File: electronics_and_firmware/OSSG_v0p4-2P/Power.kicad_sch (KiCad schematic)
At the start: 37 parts, among them J3 USB_B_Micro, Q3 PMZ290UNE2YL, Q4 EMF20B02V, SW2 Power, U4 XC61CC3002MR, U5 AP5054HTC, U6 MAX17048, U7 NCP167BMX330TBG, U8 SY7088

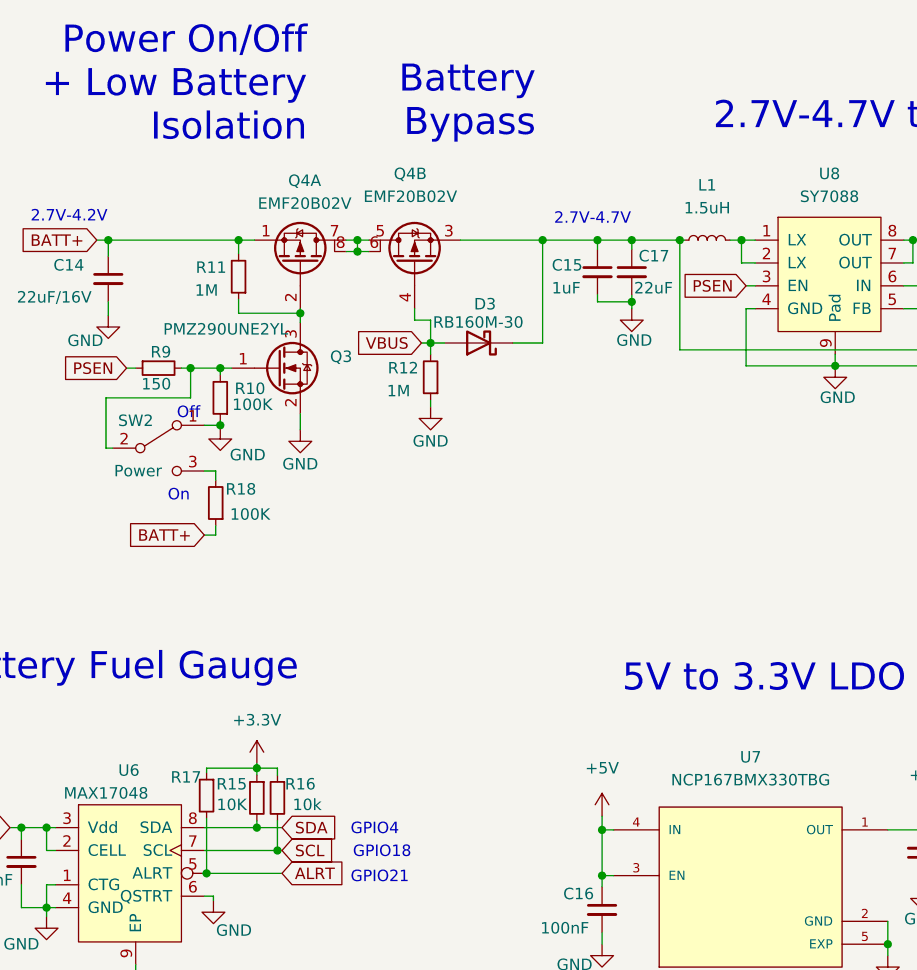
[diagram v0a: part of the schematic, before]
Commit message: V0.4 PCB nearly finished.  3D models mostly added in. Needs reviewing
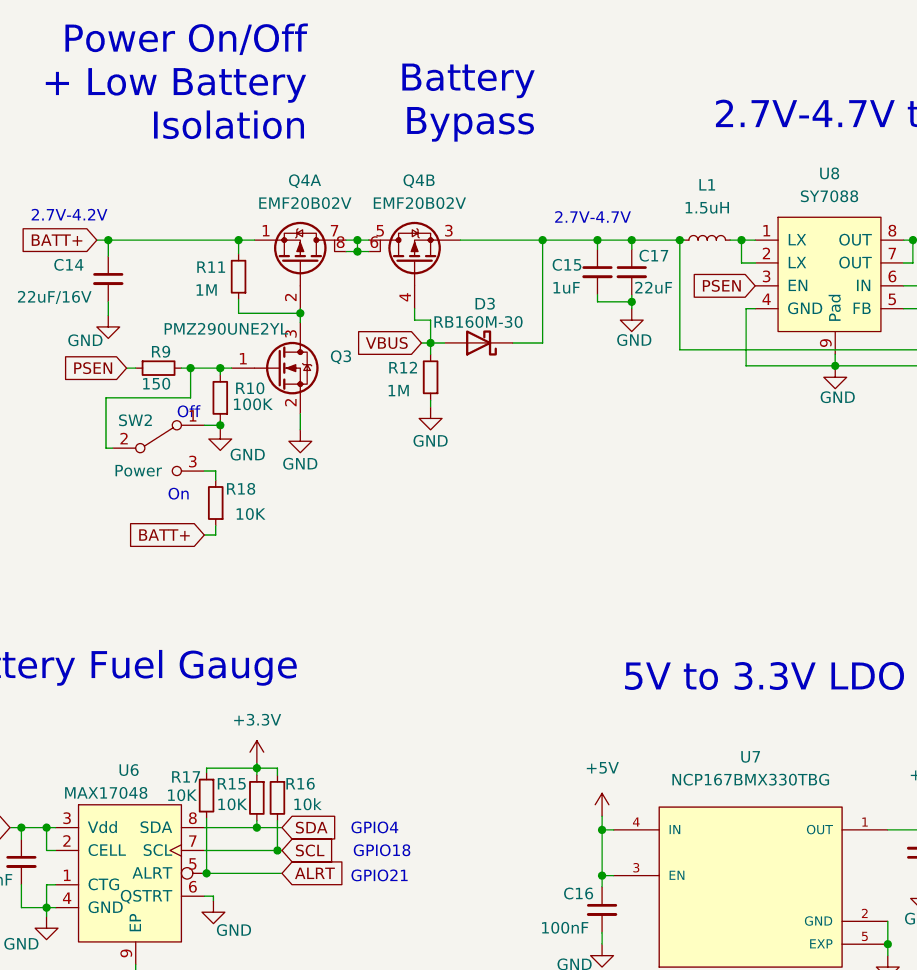
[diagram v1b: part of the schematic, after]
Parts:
- R17: value (none) -> 10K; footprint (none) -> Resistor_SMD:R_0402_1005Metric
- R18: value 100K -> 10K
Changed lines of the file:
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@@
-    (stroke (width 0) (type default) (color 0 0 0 0))
-  )
-  (wire (pts (xy 219.456 68.58) (xy 220.472 68.58))
     (stroke (width 0) (type default) (color 0 0 0 0))
   )
@@
     )
   )
-  (global_label "PSEN" (shape input) (at 219.456 68.58 180) (fields_autoplaced)
+  (global_label "PSEN" (shape input) (at 220.472 68.58 180) (fields_autoplaced)
     (effects (font (size 1.27 1.27)) (justify right))
-    (property "Intersheet References" "${INTERSHEET_REFS}" (id 0) (at 212.0839 68.5006 0)
+    (property "Intersheet References" "${INTERSHEET_REFS}" (id 0) (at 213.0999 68.5006 0)
       (effects (font (size 1.27 1.27)) (justify right) hide)
     )
@@
   )
   (symbol (lib_id "OSSG_components_lib:EMF20B02V") (at 182.626 66.04 90) (unit 2)
-    (in_bom yes) (on_board yes) (fields_autoplaced)
-    (property "Reference" "Q4" (id 0) (at 182.1434 56.134 90))
-    (property "Value" "EMF20B02V" (id 1) (at 182.1434 58.674 90))
+    (in_bom yes) (on_board yes)
+    (property "Reference" "Q4" (id 0) (at 183.134 56.896 90))
+    (property "Value" "EMF20B02V" (id 1) (at 183.134 59.436 90))
     (property "Footprint" "OSSG_footprints:EMF20B02V" (id 2) (at 182.626 64.77 0)
       (effects (font (size 1.27 1.27)) hide)
@@
     (in_bom yes) (on_board yes)
     (property "Reference" "R18" (id 0) (at 163.322 91.186 0))
-    (property "Value" "100K" (id 1) (at 164.338 93.98 0))
+    (property "Value" "10K" (id 1) (at 164.338 93.98 0))
     (property "Footprint" "Resistor_SMD:R_0402_1005Metric" (id 2) (at 160.528 92.71 0)
       (effects (font (size 1.27 1.27)) hide)
@@
     (in_bom yes) (on_board yes)
     (property "Reference" "R17" (id 0) (at 157.226 123.19 0))
-    (property "Value" "" (id 1) (at 156.718 125.222 0))
-    (property "Footprint" "" (id 2) (at 159.512 125.222 0)
-      (effects (font (size 1.27 1.27)) hide)
-    )
+    (property "Value" "10K" (id 1) (at 156.718 125.222 0))
+    (property "Footprint" "Resistor_SMD:R_0402_1005Metric" (id 2) (at 159.512 125.222 0)
+      (effects (font (size 1.27 1.27)) hide)
+    )

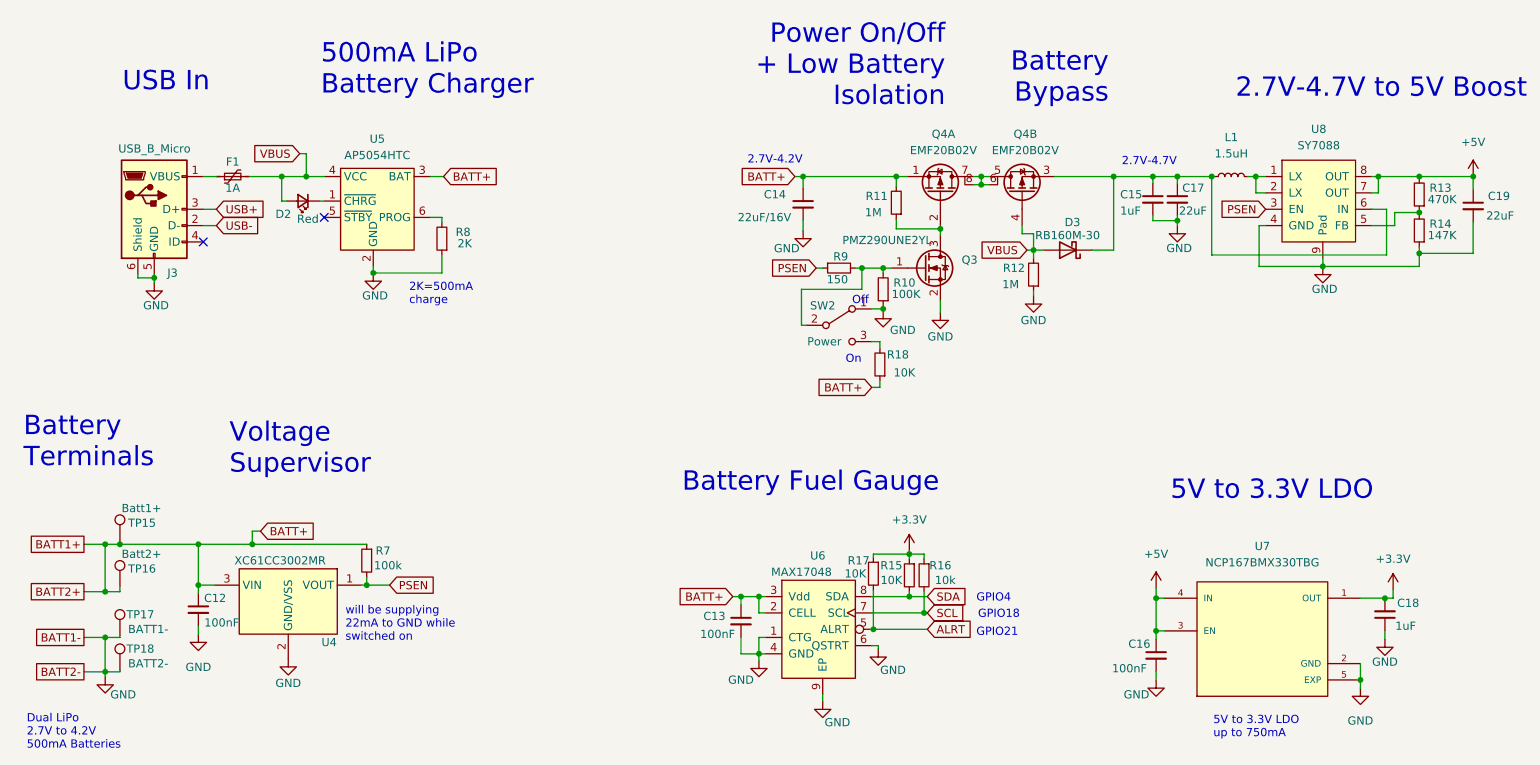
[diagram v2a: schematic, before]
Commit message: change Q4 footprint
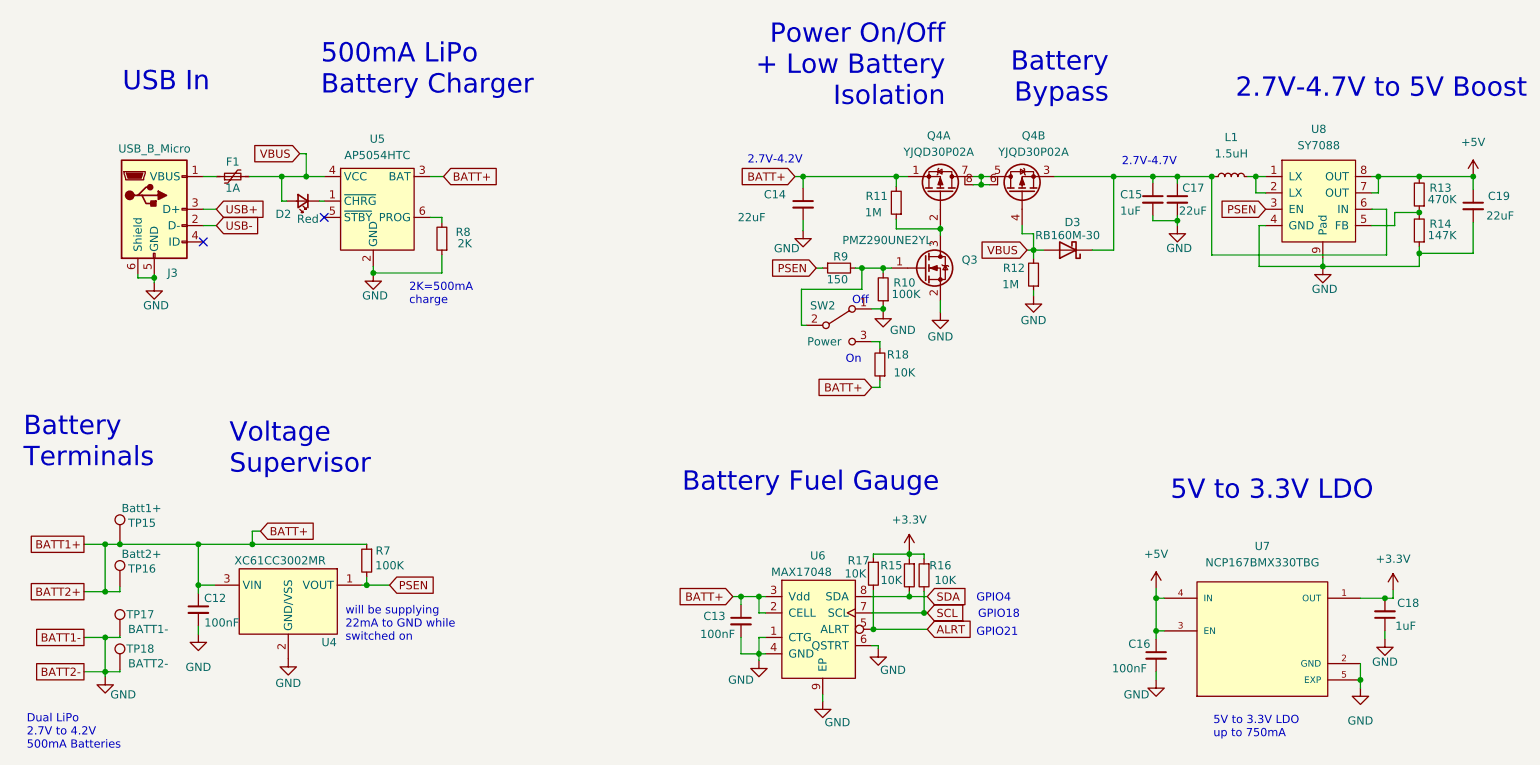
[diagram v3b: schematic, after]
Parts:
- removed Q4: EMF20B02V, OSSG_footprints:EMF20B02V, symbol OSSG_components_lib:EMF20B02V
- added Q4: YJQD30P02A, OSSG_footprints:YJQD30P02A_DFN3.3x3.3, symbol OSSG_components_lib:YJQD30P02A
- C14: value 22uF/16V -> 22uF
- R16: value 10k -> 10K
- R7: value 100k -> 100K
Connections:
- net BATT+: now also Q4.1 (S2)
- net VBUS: now also Q4.4 (G2)
- net at C15.1, C17.1, D3.1 (K)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: now also Q4.3 (S2)
- net at Q3.3 (D), R11.1: now also Q4.2 (G2)
- new net: Q4.5 (D2), Q4.6 (D2), Q4.7 (D2), Q4.8 (D2)
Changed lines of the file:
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@@
   (title_block
     (title "Team OpenSource Smartglasses")
-    (date "2022-09-18")
-    (rev "V0.4b4")
+    (date "2022-09-19")
+    (rev "V0.4b5")
     (comment 1 "2P Battery Version")
     (comment 2 "MIT License")
@@
     (pin "1")
   )
-  (symbol (lib_id "OSSG_components_lib:EMF20B02V") (at 169.926 66.04 270) (mirror x) (unit 1)
-    (in_bom yes) (on_board yes) (fields_autoplaced)
-    (property "Reference" "Q4" (id 0) (at 170.4086 56.896 90))
-    (property "Value" "EMF20B02V" (id 1) (at 170.4086 59.436 90))
-    (property "Footprint" "OSSG_footprints:EMF20B02V" (id 2) (at 169.926 64.77 0)
-      (effects (font (size 1.27 1.27)) hide)
-    )
-    (property "Datasheet" "~" (id 3) (at 169.926 64.77 0)
-      (effects (font (size 1.27 1.27)) hide)
-    )
-    (pin "1")
-    (pin "2")
-    (pin "7")
-    (pin "8")
-    (pin "3")
-    (pin "4")
-    (pin "5")
-    (pin "6")
-  )
   (symbol (lib_id "Device:C_Small") (at 138.938 132.588 0) (unit 1)
     (in_bom yes) (on_board yes)
@@
     (in_bom yes) (on_board yes)
     (property "Reference" "R16" (id 0) (at 169.926 123.952 0))
-    (property "Value" "10k" (id 1) (at 170.688 126.238 0))
+    (property "Value" "10K" (id 1) (at 170.688 126.238 0))
     (property "Footprint" "Resistor_SMD:R_0402_1005Metric" (id 2) (at 167.386 125.476 0)
       (effects (font (size 1.27 1.27)) hide)
@@
     (pin "1")
   )
-  (symbol (lib_id "OSSG_components_lib:EMF20B02V") (at 182.626 66.04 90) (unit 2)
-    (in_bom yes) (on_board yes)
-    (property "Reference" "Q4" (id 0) (at 183.134 56.896 90))
-    (property "Value" "EMF20B02V" (id 1) (at 183.134 59.436 90))
-    (property "Footprint" "OSSG_footprints:EMF20B02V" (id 2) (at 182.626 64.77 0)
+  (symbol (lib_id "OSSG_components_lib:YJQD30P02A") (at 182.626 66.04 90) (unit 2)
+    (in_bom yes) (on_board yes)
+    (property "Reference" "Q4" (id 0) (at 184.404 57.15 90))
+    (property "Value" "YJQD30P02A" (id 1) (at 184.404 59.69 90))
+    (property "Footprint" "OSSG_footprints:YJQD30P02A_DFN3.3x3.3" (id 2) (at 182.626 64.77 0)
       (effects (font (size 1.27 1.27)) hide)
     )
@@
     (in_bom yes) (on_board yes)
     (property "Reference" "R7" (id 0) (at 83.312 121.666 0))
-    (property "Value" "100k" (id 1) (at 84.074 123.952 0))
+    (property "Value" "100K" (id 1) (at 84.328 123.952 0))
     (property "Footprint" "Resistor_SMD:R_0402_1005Metric" (id 2) (at 80.772 123.19 0)
       (effects (font (size 1.27 1.27)) hide)
@@
     (pin "2")
   )
-  (symbol (lib_id "power:GND") (at 169.926 84.582 0) (unit 1)
-    (in_bom yes) (on_board yes)
-    (property "Reference" "#PWR037" (id 0) (at 169.926 90.932 0)
-      (effects (font (size 1.27 1.27)) hide)
-    )
-    (property "Value" "GND" (id 1) (at 169.926 88.392 0))
-    (property "Footprint" "" (id 2) (at 169.926 84.582 0)
-      (effects (font (size 1.27 1.27)) hide)
-    )
-    (property "Datasheet" "" (id 3) (at 169.926 84.582 0)
-      (effects (font (size 1.27 1.27)) hide)
-    )
-    (pin "1")
-  )
-  (symbol (lib_id "Connector:USB_B_Micro") (at 47.752 68.58 0) (unit 1)
-    (in_bom yes) (on_board yes)
-    (property "Reference" "J3" (id 0) (at 49.784 78.486 0)
-      (effects (font (size 1.27 1.27)) (justify left))
-    )
-    (property "Value" "USB_B_Micro" (id 1) (at 42.164 59.182 0)
-      (effects (font (size 1.27 1.27)) (justify left))
-    )
-    (property "Footprint" "Connector_USB:USB_Micro-B_Amphenol_10118194_Horizontal" (id 2) (at 51.562 69.85 0)
-      (effects (font (size 1.27 1.27)) hide)
-    )
-    (property "Datasheet" "https://www.molex.com/pdm_docs/sd/1050170001_sd.pdf" (id 3) (at 51.562 69.85 0)
-      (effects (font (size 1.27 1.27)) hide)
-    )
-    (property "MPN" "WM1399CT-ND" (id 4) (at 47.752 68.58 90)
-      (effects (font (size 1.27 1.27)) hide)
-    )
-    (property "Price" "1.33" (id 5) (at 47.752 68.58 90)
-      (effects (font (size 1.27 1.27)) hide)
-    )
-    (property "DigiKeyLink" "https://www.digikey.ca/en/products/detail/molex/1050170001/2350832" (id 6) (at 47.752 68.58 90)
-      (effects (font (size 1.27 1.27)) hide)
-    )
-    (property "Price_LCSC" "0.244" (id 7) (at 47.752 68.58 90)
-      (effects (font (size 1.27 1.27)) hide)
-    )
-    (property "LinkLCSC" "https://lcsc.com/product-detail/USB-Connectors_MOLEX-1050170001_C136000.html" (id 8) (at 47.752 68.58 90)
-      (effects (font (size 1.27 1.27)) hide)
-    )
-    (property "MPN_LCSC" "C136000" (id 9) (at 47.752 68.58 90)
-      (effects (font (size 1.27 1.27)) hide)
-    )
-    (pin "1")
-    (pin "2")
+  (symbol (lib_id "OSSG_components_lib:YJQD30P02A") (at 169.926 66.04 270) (mirror x) (unit 1)
+    (in_bom yes) (on_board yes)
+    (property "Reference" "Q4" (id 0) (at 169.672 57.15 90))
+    (property "Value" "YJQD30P02A" (id 1) (at 169.672 59.69 90))
+    (property "Footprint" "OSSG_footprints:YJQD30P02A_DFN3.3x3.3" (id 2) (at 169.926 64.77 0)
+      (effects (font (size 1.27 1.27)) hide)
+    )
+    (property "Datasheet" "~" (id 3) (at 169.926 64.77 0)
+      (effects (font (size 1.27 1.27)) hide)
+    )
+    (pin "1")
+    (pin "2")
+    (pin "7")
+    (pin "8")
     (pin "3")
     (pin "4")
@@
     (pin "6")
   )
+  (symbol (lib_id "power:GND") (at 169.926 84.582 0) (unit 1)
+    (in_bom yes) (on_board yes)
+    (property "Reference" "#PWR037" (id 0) (at 169.926 90.932 0)
+      (effects (font (size 1.27 1.27)) hide)
+    )
+    (property "Value" "GND" (id 1) (at 169.926 88.392 0))
+    (property "Footprint" "" (id 2) (at 169.926 84.582 0)
+      (effects (font (size 1.27 1.27)) hide)
+    )
+    (property "Datasheet" "" (id 3) (at 169.926 84.582 0)
+      (effects (font (size 1.27 1.27)) hide)
+    )
+    (pin "1")
+  )
+  (symbol (lib_id "Connector:USB_B_Micro") (at 47.752 68.58 0) (unit 1)
+    (in_bom yes) (on_board yes)
+    (property "Reference" "J3" (id 0) (at 49.784 78.486 0)
+      (effects (font (size 1.27 1.27)) (justify left))
+    )
+    (property "Value" "USB_B_Micro" (id 1) (at 42.164 59.182 0)
+      (effects (font (size 1.27 1.27)) (justify left))
+    )
+    (property "Footprint" "Connector_USB:USB_Micro-B_Amphenol_10118194_Horizontal" (id 2) (at 51.562 69.85 0)
+      (effects (font (size 1.27 1.27)) hide)
+    )
+    (property "Datasheet" "https://www.molex.com/pdm_docs/sd/1050170001_sd.pdf" (id 3) (at 51.562 69.85 0)
+      (effects (font (size 1.27 1.27)) hide)
+    )
+    (property "MPN" "WM1399CT-ND" (id 4) (at 47.752 68.58 90)
+      (effects (font (size 1.27 1.27)) hide)
+    )
+    (property "Price" "1.33" (id 5) (at 47.752 68.58 90)
+      (effects (font (size 1.27 1.27)) hide)
+    )
+    (property "DigiKeyLink" "https://www.digikey.ca/en/products/detail/molex/1050170001/2350832" (id 6) (at 47.752 68.58 90)
+      (effects (font (size 1.27 1.27)) hide)
+    )
+    (property "Price_LCSC" "0.244" (id 7) (at 47.752 68.58 90)
+      (effects (font (size 1.27 1.27)) hide)
+    )
+    (property "LinkLCSC" "https://lcsc.com/product-detail/USB-Connectors_MOLEX-1050170001_C136000.html" (id 8) (at 47.752 68.58 90)
+      (effects (font (size 1.27 1.27)) hide)
+    )
+    (property "MPN_LCSC" "C136000" (id 9) (at 47.752 68.58 90)
+      (effects (font (size 1.27 1.27)) hide)
+    )
+    (pin "1")
+    (pin "2")
+    (pin "3")
+    (pin "4")
+    (pin "5")
+    (pin "6")
+  )
   (symbol (lib_id "power:GND") (at 239.014 135.382 0) (unit 1)
     (in_bom yes) (on_board yes)
@@
       (effects (font (size 1.27 1.27)) (justify left))
     )
-    (property "Value" "22uF/16V" (id 1) (at 138.43 69.85 0)
-      (effects (font (size 1.27 1.27)) (justify left))
-    )
+    (property "Value" "22uF" (id 1) (at 138.43 69.85 0)
+      (effects (font (size 1.27 1.27)) (justify left))
+    )

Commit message: updating schematic and PCB with minor changes
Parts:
- R15, R16: value 10K -> 4.7K
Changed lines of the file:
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@@
   (title_block
     (title "Team OpenSource Smartglasses")
-    (date "2022-09-19")
-    (rev "V0.4b5")
+    (date "2022-10-14")
+    (rev "V0.4a")
     (comment 1 "2P Battery Version")
     (comment 2 "MIT License")
@@
     (in_bom yes) (on_board yes)
     (property "Reference" "R15" (id 0) (at 162.306 123.952 0))
-    (property "Value" "10K" (id 1) (at 162.306 126.238 0))
+    (property "Value" "4.7K" (id 1) (at 162.306 126.238 0))
     (property "Footprint" "Resistor_SMD:R_0402_1005Metric" (id 2) (at 165.1 125.476 0)
       (effects (font (size 1.27 1.27)) hide)
@@
     (in_bom yes) (on_board yes)
     (property "Reference" "R16" (id 0) (at 169.926 123.952 0))
-    (property "Value" "10K" (id 1) (at 170.688 126.238 0))
+    (property "Value" "4.7K" (id 1) (at 170.688 126.238 0))
     (property "Footprint" "Resistor_SMD:R_0402_1005Metric" (id 2) (at 167.386 125.476 0)
       (effects (font (size 1.27 1.27)) hide)

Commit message: updated KiCAD V0.4 and V0.5 schematics with correct switch part number
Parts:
- SW2: P/N C145858 -> C145857
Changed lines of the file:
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@@
       (effects (font (size 1.27 1.27)) hide)
     )
-    (property "P/N" "C145858" (id 4) (at 154.178 86.614 0)
+    (property "P/N" "C145857" (id 4) (at 154.178 86.614 0)
       (effects (font (size 1.27 1.27)) hide)
     )
